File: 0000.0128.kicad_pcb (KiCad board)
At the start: 2 copper layers, 168 x 45.7 mm, 76 parts, among them J1 MicroMatch, J2 MicroMatch, J3 MicroMatch, J4 MicroMatch, J5 MicroMatch, J6 MicroMatch, J7 MicroMatch, J8 MicroMatch, U1 TL072, U2 TL072, U3 TL072, U4 TL072, U5 TL072, U6 TL072

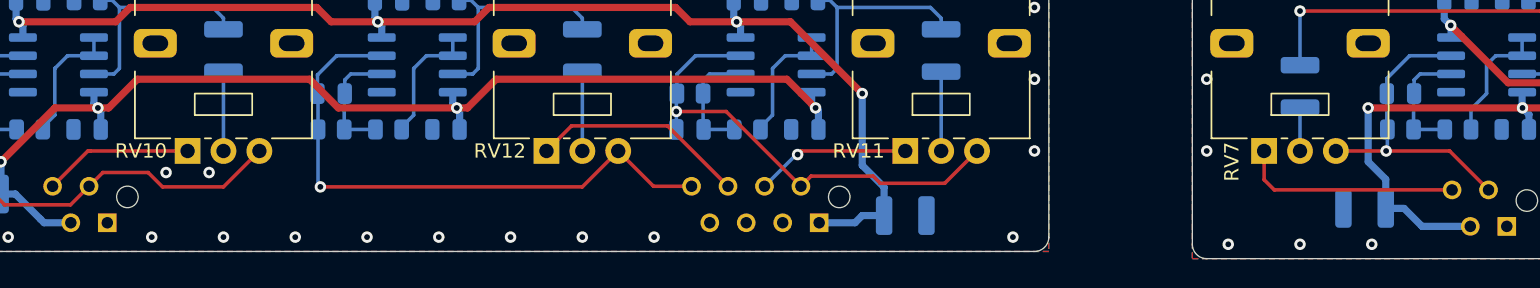
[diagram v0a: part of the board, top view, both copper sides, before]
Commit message: Oops, all of the single gang pots were backwards - fixed.
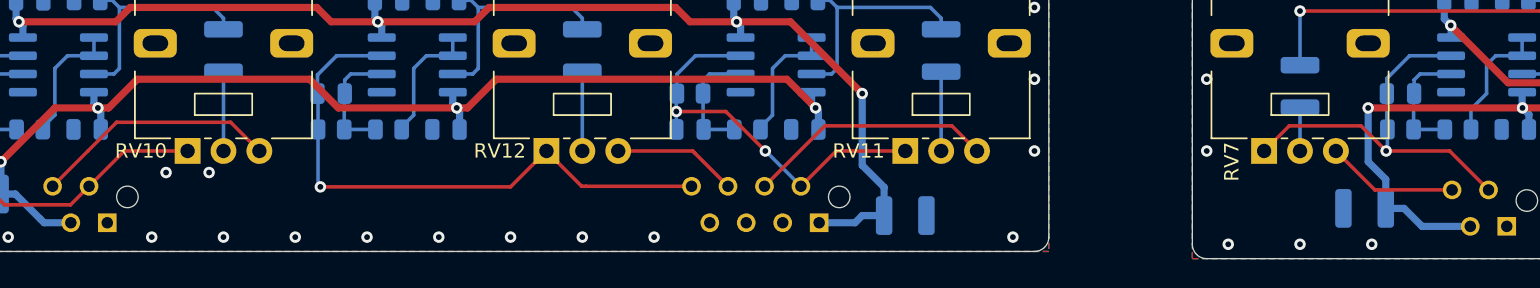
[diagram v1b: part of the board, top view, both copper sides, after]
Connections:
- RV10 pad 1: /Variant 4/SUB_IN -> /Variant 4/SUB_OUT
- RV10 pad 3: /Variant 4/SUB_OUT -> /Variant 4/SUB_IN
- RV11 pad 1: /Variant 4/CH1_IN -> /Variant 4/CH1_OUT
- RV11 pad 3: /Variant 4/CH1_OUT -> /Variant 4/CH1_IN
- RV12 pad 1: /Variant 4/CH2_IN -> /Variant 4/CH2_OUT
- RV12 pad 3: /Variant 4/CH2_OUT -> /Variant 4/CH2_IN
- RV7 pad 1: /Variant 3/SUB_IN -> /Variant 3/SUB_OUT
- RV7 pad 3: /Variant 3/SUB_OUT -> /Variant 3/SUB_IN
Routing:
- net /Variant 4/SUB_IN: track 10.4 -> 17.1 mm
- net /Variant 4/CH2_IN: track 15.1 -> 8.67 mm
- net /Variant 4/CH1_IN: track 10.8 -> 17.3 mm, vias 1 -> 0
- net /Variant 3/SUB_OUT: track 22.0 -> 28.4 mm
- net /Variant 3/SUB_IN: track 15.4 -> 9.22 mm
- net /Variant 4/SUB_OUT: track 35.5 -> 29.7 mm
- net /Variant 4/CH1_OUT: track 33.4 -> 28.0 mm, vias 1 -> 2
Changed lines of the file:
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@@
 			)
 			(remove_unused_layers no)
-			(net 76 "/Variant 4/SUB_IN")
+			(net 62 "/Variant 4/SUB_OUT")
 			(pinfunction "1")
 			(pintype "passive")
@@
 			)
 			(remove_unused_layers no)
-			(net 62 "/Variant 4/SUB_OUT")
+			(net 76 "/Variant 4/SUB_IN")
 			(pinfunction "3")
 			(pintype "passive")
@@
 			)
 			(remove_unused_layers no)
-			(net 32 "/Variant 3/SUB_IN")
+			(net 11 "/Variant 3/SUB_OUT")
 			(pinfunction "1")
 			(pintype "passive")
@@
 			)
 			(remove_unused_layers no)
-			(net 11 "/Variant 3/SUB_OUT")
+			(net 32 "/Variant 3/SUB_IN")
 			(pinfunction "3")
 			(pintype "passive")
@@
 			)
 			(remove_unused_layers no)
-			(net 74 "/Variant 4/CH2_IN")
+			(net 70 "/Variant 4/CH2_OUT")
 			(pinfunction "1")
 			(pintype "passive")
@@
 			)
 			(remove_unused_layers no)
-			(net 70 "/Variant 4/CH2_OUT")
+			(net 74 "/Variant 4/CH2_IN")
 			(pinfunction "3")
 			(pintype "passive")
@@
 			)
 			(remove_unused_layers no)
-			(net 75 "/Variant 4/CH1_IN")
+			(net 68 "/Variant 4/CH1_OUT")
 			(pinfunction "1")
 			(pintype "passive")
@@
 			)
 			(remove_unused_layers no)
-			(net 68 "/Variant 4/CH1_OUT")
+			(net 75 "/Variant 4/CH1_IN")
 			(pinfunction "3")
 			(pintype "passive")
@@
 		(tags "resistor")
 		(property "Reference" "R19"
-			(at 0 -1.75 0)
+			(at 0.5 -1.75 0)
 			(layer "B.SilkS")
 			(effects
@@
 	)
 	(segment
+		(start 152.5 110)
+		(end 154.25 108.25)
+		(width 0.25)
+		(layer "F.Cu")
+		(net 11)
+	)
+	(segment
 		(start 161 110)
 		(end 165.4225 110)
@@
 	)
 	(segment
-		(start 157.5 110)
+		(start 159.25 108.25)
 		(end 161 110)
 		(width 0.25)
@@
 		(net 11)
 	)
+	(segment
+		(start 154.25 108.25)
+		(end 159.25 108.25)
+		(width 0.25)
+		(layer "F.Cu")
+		(net 11)
+	)
 	(via
 		(at 161 110)
@@
 	)
 	(segment
-		(start 152.5 112)
-		(end 152.5 110)
-		(width 0.25)
-		(layer "F.Cu")
-		(net 32)
-	)
-	(segment
-		(start 165.595 112.7125)
-		(end 153.2125 112.7125)
+		(start 157.5 110)
+		(end 160.2125 112.7125)
 		(width 0.25)
 		(layer "F.Cu")
@@
 	)
 	(segment
-		(start 153.2125 112.7125)
-		(end 152.5 112)
+		(start 160.2125 112.7125)
+		(end 165.595 112.7125)
 		(width 0.25)
 		(layer "F.Cu")
@@
 	)
 	(segment
-		(start 71.595 111.5)
-		(end 74.75 111.5)
-		(width 0.25)
-		(layer "F.Cu")
-		(net 62)
-	)
-	(segment
-		(start 74.75 111.5)
-		(end 75.75 112.5)
-		(width 0.25)
-		(layer "F.Cu")
-		(net 62)
-	)
-	(segment
 		(start 70.635 112.46)
 		(end 69.345 113.75)
@@
 	)
 	(segment
-		(start 64.75 113.75)
-		(end 61.75 110.75)
-		(width 0.25)
-		(layer "F.Cu")
-		(net 62)
-	)
-	(segment
-		(start 75.75 112.5)
-		(end 80 112.5)
+		(start 77.5 110)
+		(end 73.095 110)
 		(width 0.25)
 		(layer "F.Cu")
@@
 	)
 	(segment
-		(start 80 112.5)
-		(end 82.5 110)
+		(start 64.75 113.75)
+		(end 61.75 110.75)
 		(width 0.25)
 		(layer "F.Cu")
@@
 	)
 	(segment
-		(start 70.635 112.46)
-		(end 71.595 111.5)
+		(start 73.095 110)
+		(end 70.635 112.46)
 		(width 0.25)
 		(layer "F.Cu")
@@
 	)
 	(segment
-		(start 120.94 111.75)
-		(end 125.25 111.75)
-		(width 0.25)
-		(layer "F.Cu")
-		(net 68)
-	)
-	(segment
-		(start 130.25 112.25)
-		(end 132.5 110)
+		(start 115 107.25)
+		(end 111.55 107.25)
 		(width 0.25)
 		(layer "F.Cu")
@@
 	)
 	(segment
-		(start 120.23 112.46)
-		(end 115.02 107.25)
+		(start 117.75 110)
+		(end 115 107.25)
 		(width 0.25)
 		(layer "F.Cu")
@@
 	)
 	(segment
-		(start 115.02 107.25)
-		(end 111.55 107.25)
+		(start 127.5 110)
+		(end 122.69 110)
 		(width 0.25)
 		(layer "F.Cu")
@@
 	)
 	(segment
-		(start 125.75 112.25)
-		(end 130.25 112.25)
+		(start 122.69 110)
+		(end 120.23 112.46)
 		(width 0.25)
 		(layer "F.Cu")
@@
 	)
 	(segment
-		(start 125.25 111.75)
-		(end 125.75 112.25)
+		(start 117.77 110)
+		(end 117.75 110)
 		(width 0.25)
 		(layer "F.Cu")
 		(net 68)
 	)
-	(segment
-		(start 120.23 112.46)
-		(end 120.94 111.75)
-		(width 0.25)
-		(layer "F.Cu")
+	(via
+		(at 111.55 107.25)
+		(size 0.8)
+		(drill 0.4)
+		(layers "F.Cu" "B.Cu")
 		(net 68)
 	)
 	(via
-		(at 111.55 107.25)
+		(at 117.75 110)
 		(size 0.8)
 		(drill 0.4)
@@
 	)
 	(segment
+		(start 117.77 110)
+		(end 120.23 112.46)
+		(width 0.25)
+		(layer "B.Cu")
+		(net 68)
+	)
+	(segment
 		(start 112.885 103.365)
 		(end 116.025 103.365)
@@
 	)
 	(segment
+		(start 117.75 110)
+		(end 117.77 110)
+		(width 0.25)
+		(layer "B.Cu")
+		(net 68)
+	)
+	(segment
 		(start 113.45 108.5)
 		(end 115.5875 108.5)
@@
 	)
 	(segment
-		(start 86.75 112.5)
-		(end 105 112.5)
+		(start 105.25 112.46)
+		(end 112.61 112.46)
 		(width 0.25)
 		(layer "F.Cu")
@@
 	)
 	(segment
-		(start 109.96 112.46)
-		(end 112.61 112.46)
+		(start 104.96 112.46)
+		(end 105.25 112.46)
 		(width 0.25)
 		(layer "F.Cu")
@@
 	)
 	(segment
-		(start 105 112.5)
-		(end 107.5 110)
+		(start 102.5 110)
+		(end 100 112.5)
 		(width 0.25)
 		(layer "F.Cu")
@@
 	)
 	(segment
-		(start 107.5 110)
-		(end 109.96 112.46)
+		(start 86.75 112.5)
+		(end 100 112.5)
+		(width 0.25)
+		(layer "F.Cu")
+		(net 70)
+	)
+	(segment
+		(start 102.5 110)
+		(end 104.96 112.46)
 		(width 0.25)
 		(layer "F.Cu")
@@
 	)
 	(segment
-		(start 104.25 108.25)
-		(end 102.5 110)
+		(start 107.5 110)
+		(end 112.69 110)
 		(width 0.25)
 		(layer "F.Cu")
@@
 	)
 	(segment
-		(start 110.94 108.25)
-		(end 104.25 108.25)
+		(start 115.15 112.46)
+		(end 112.845 110.155)
 		(width 0.25)
 		(layer "F.Cu")
@@
 	)
 	(segment
-		(start 115.15 112.46)
-		(end 110.94 108.25)
+		(start 112.69 110)
+		(end 112.845 110.155)
 		(width 0.25)
 		(layer "F.Cu")
@@
 	)
 	(segment
-		(start 120 110.25)
-		(end 120.25 110)
+		(start 130.75 108.25)
+		(end 132.5 110)
 		(width 0.25)
 		(layer "F.Cu")
@@
 	)
 	(segment
-		(start 120.25 110)
-		(end 127.5 110)
+		(start 121.9 108.25)
+		(end 130.75 108.25)
 		(width 0.25)
 		(layer "F.Cu")
 		(net 75)
 	)
-	(via
-		(at 120 110.25)
-		(size 0.8)
-		(drill 0.4)
-		(layers "F.Cu" "B.Cu")
-		(net 75)
-	)
 	(segment
-		(start 119.9 110.25)
-		(end 120 110.25)
+		(start 117.69 112.46)
+		(end 121.9 108.25)
 		(width 0.25)
-		(layer "B.Cu")
+		(layer "F.Cu")
 		(net 75)
 	)
 	(segment
-		(start 117.69 112.46)
-		(end 119.9 110.25)
+		(start 82.5 110)
+		(end 80.5 108)
 		(width 0.25)
-		(layer "B.Cu")
-		(net 75)
+		(layer "F.Cu")
+		(net 76)
 	)
 	(segment
-		(start 70.555 110)
-		(end 70.75 110)
+		(start 72.555 108)
+		(end 70.555 110)
 		(width 0.25)
 		(layer "F.Cu")
@@
 	)
 	(segment
-		(start 77.5 110)
-		(end 70.75 110)
+		(start 80.5 108)
+		(end 72.555 108)
 		(width 0.25)
 		(layer "F.Cu")

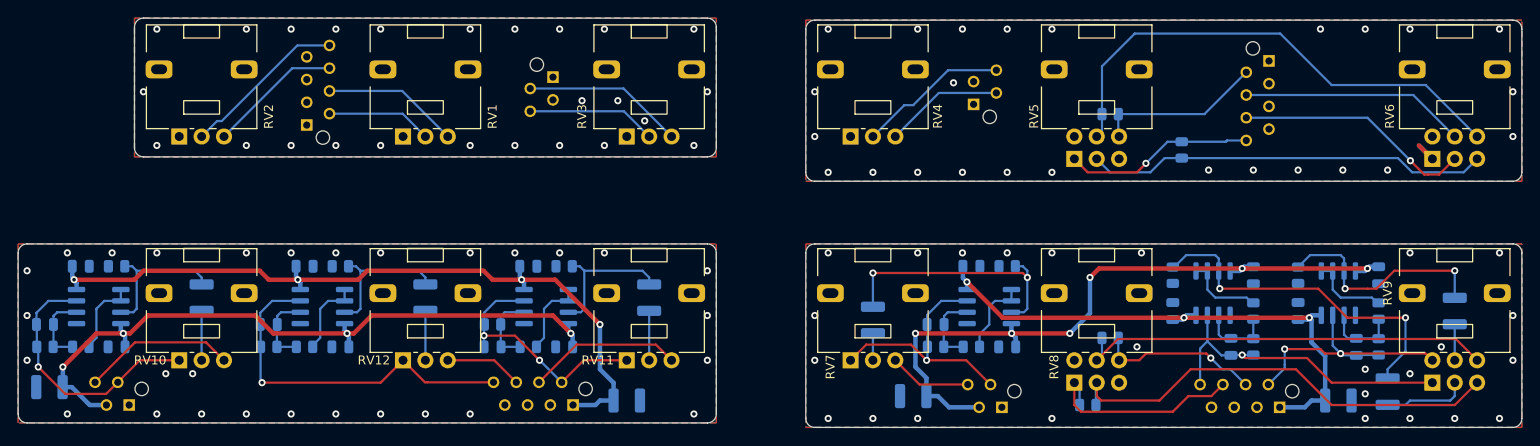
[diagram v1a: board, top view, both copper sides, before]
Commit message: Active control topology changed to a single op-amp version.
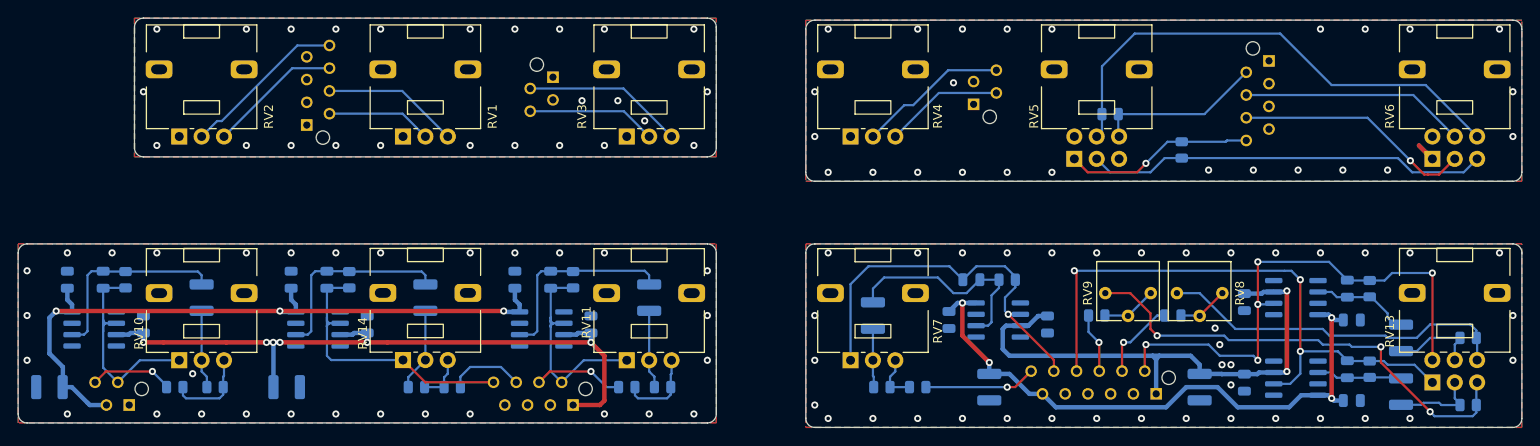
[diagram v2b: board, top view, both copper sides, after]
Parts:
- removed C27, C28: 151, Capacitor_SMD:C_0805_2012Metric
- removed J5: MicroMatch, Connector_TE-Connectivity:TE_Micro-MaTch_215079-8_2x04_P1.27mm_Vertical
- removed J6: MicroMatch, Connector_TE-Connectivity:TE_Micro-MaTch_215079-4_2x02_P1.27mm_Vertical
- removed R20: 3K, Resistor_SMD:R_0805_2012Metric
- removed R21, R22: 15K, Resistor_SMD:R_0805_2012Metric
- removed RV12: 10K, Potentiometer_THT:Potentiometer_Alps_RK09L_Single_Vertical
- removed U4, U5, U6: TL072, Package_SO:SOIC-8_3.9x4.9mm_P1.27mm
- added C29: 106, Capacitor_SMD:C_1210_3225Metric, B.Cu at (105.0, 103.0)
- added C30: 151, Capacitor_SMD:C_0805_2012Metric, B.Cu at (94.0, 101.0)
- added J9: MicroMatch, Connector_TE-Connectivity:TE_Micro-MaTch_1-215079-2_2x06_P1.27mm_Vertical, B.Cu at (186.6, 113.8)
- added R23: 100K, Resistor_SMD:R_0805_2012Metric, B.Cu at (96.5, 101.0)
- added RV13: 10K, Potentiometer_THT:Potentiometer_Alps_RK09L_Double_Vertical, F.Cu at (217.5, 112.5)
- added RV14: 10K LIN, Potentiometer_THT:Potentiometer_Alps_RK09L_Single_Vertical, F.Cu at (102.5, 110.0)
- added U7: TL071, Package_SO:SOIC-8_3.9x4.9mm_P1.27mm, B.Cu at (93.0, 106.5)
- added U8: TL071, Package_SO:SOIC-8_3.9x4.9mm_P1.27mm, B.Cu at (68.0, 106.5)
- added U9: TL071, Package_SO:SOIC-8_3.9x4.9mm_P1.27mm, B.Cu at (118.0, 106.5)
- C1, C11, C12, C15, C25: value 105 -> 106
- C26: value 105 -> 151; footprint Capacitor_SMD:C_1210_3225Metric -> Capacitor_SMD:C_0805_2012Metric
- R10, R11, R19: value 3K -> 100K
- R12: value 15K -> 3K
- R13, R5: value 15K -> 22K
- R14, R17: value 100K -> 3K
- R15: value 3K -> 22K
- R16: value 15K -> 100K
- R18, R8, R9: value 100K -> 22K
- R6, R7: value R -> 3K
- RV10, RV11, RV7: value 10K -> 10K LIN
- RV8, RV9: value 10K -> 1K; footprint Potentiometer_THT:Potentiometer_Alps_RK09L_Double_Vertical -> HR_parts:Potentiometer_Bourns_3362P_Vertical
- U1, U2, U3: value TL072 -> TL071
- moved R12 103.6 mm to (108.0, 113.0), turned to 180 degrees
- moved R13 93.6 mm to (104.0, 113.0), turned to 180 degrees
- moved R18 38.4 mm to (131.5, 113.0), turned to 180 degrees
- moved C23 38.0 mm to (89.5, 113.0)
- moved R9 36.0 mm to (221.5, 115.0), turned to 180 degrees
- moved RV9 35.4 mm to (183.5, 102.5), turned to -90 degrees
- moved R8 20.2 mm to (221.5, 107.5), turned to 180 degrees
- moved C4 17.8 mm to (208.5, 114.5), turned to 180 degrees
- moved RV8 17.2 mm to (191.5, 102.5), turned to -90 degrees
- moved R15 15.7 mm to (81.5, 113.0)
- moved C9 15.6 mm to (191.5, 113.0), turned to -90 degrees
- moved R17 15.2 mm to (127.5, 113.0)
- moved R14 15.0 mm to (77.0, 113.0)
- moved R11 14.5 mm to (210.5, 111.0)
- moved C26 14.1 mm to (119.0, 101.0), turned to -90 degrees
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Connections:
- C1 pad 2: Net-(U1A-+) -> Net-(U1--)
- C11 pad 2: Net-(U2A-+) -> Net-(U2--)
- C12 pad 2: Net-(U3A-+) -> Net-(U3--)
- C13 pad 1: Net-(U2B--) -> Net-(U2--)
- C14 pad 1: Net-(U3B--) -> Net-(U3--)
- C15 pad 2: Net-(U4A-+) -> Net-(U8--)
- C16 pad 1: Net-(U4B--) -> Net-(U8--)
- C2 pad 1: Net-(U1B--) -> Net-(U1--)
- C25 pad 2: Net-(U5A-+) -> Net-(U9--)
- C26 pad 1: Net-(C26-Pad1) -> Net-(U9--)
- C26 pad 2: Net-(U6A-+) -> /Variant 4/CH1_OUT
- R10 pad 1: Net-(U2A--) -> /Variant 3/CH1_OUT
- R10 pad 2: Net-(U2B--) -> Net-(U2--)
- R11 pad 1: Net-(U3A--) -> /Variant 3/CH2_OUT
- R11 pad 2: Net-(U3B--) -> Net-(U3--)
- R12 pad 1: Net-(U2B--) -> /Variant 4/CH2_IN
- R12 pad 2: /Variant 3/CH1_OUT -> Net-(R12-Pad2)
- R13 pad 1: Net-(U3B--) -> Net-(R12-Pad2)
- R13 pad 2: /Variant 3/CH2_OUT -> Net-(C29-Pad1)
- R14 pad 1: GND3 -> /Variant 4/SUB_IN
- R14 pad 2: Net-(U4A-+) -> Net-(R14-Pad2)
- R15 pad 1: Net-(U4A--) -> Net-(R14-Pad2)
- R15 pad 2: Net-(U4B--) -> Net-(C15-Pad1)
- R16 pad 1: Net-(U4B--) -> /Variant 4/SUB_OUT
- R16 pad 2: /Variant 4/SUB_OUT -> Net-(U8--)
- R17 pad 1: GND3 -> /Variant 4/CH1_IN
- R17 pad 2: Net-(U5A-+) -> Net-(R17-Pad2)
- R18 pad 1: GND3 -> Net-(R17-Pad2)
- R18 pad 2: Net-(U6A-+) -> Net-(C25-Pad1)
- R19 pad 1: Net-(U5A--) -> /Variant 4/CH1_OUT
- R19 pad 2: Net-(U5B--) -> Net-(U9--)
- R3 pad 1: GND1 -> /Variant 3/SUB_OUT
- R3 pad 2: Net-(U1A-+) -> Net-(U1--)
- R4 pad 1: Net-(U1A--) -> /Variant 3/SUB_IN
- R4 pad 2: Net-(U1B--) -> Net-(R4-Pad2)
- R5 pad 1: Net-(U1B--) -> Net-(R4-Pad2)
- R5 pad 2: /Variant 3/SUB_OUT -> Net-(C1-Pad1)
- R8 pad 1: GND1 -> Net-(R8-Pad1)
- R8 pad 2: Net-(U2A-+) -> Net-(C11-Pad1)
- R9 pad 1: GND1 -> Net-(R9-Pad1)
- R9 pad 2: Net-(U3A-+) -> Net-(C12-Pad1)
- RV10 pad 3: /Variant 4/SUB_IN -> Net-(R14-Pad2)
- RV11 pad 3: /Variant 4/CH1_IN -> Net-(R17-Pad2)
- RV7 pad 3: /Variant 3/SUB_IN -> Net-(R4-Pad2)
- RV8 pad 1: /Variant 3/CH2_IN -> Net-(R8-Pad1)
- RV8 pad 2: Net-(R7-Pad2) -> Net-(R6-Pad2)
- RV8 pad 3: GND1 -> Net-(R6-Pad2)
- RV9 pad 1: /Variant 3/CH2_OUT -> Net-(R9-Pad1)
- RV9 pad 2: Net-(C12-Pad1) -> Net-(R7-Pad2)
- U1 pad 1: Net-(U1A--) -> unconnected-(U1-NULL-Pad1)
- U1 pad 2: Net-(U1A--) -> Net-(U1--)
- U1 pad 3: Net-(U1A-+) -> GND1
- U1 pad 5: GND1 -> unconnected-(U1-NULL-Pad5)
- U1 pad 6: Net-(U1B--) -> /Variant 3/SUB_OUT
- U1 pad 7: /Variant 3/SUB_OUT -> +15V
- U1 pad 8: +15V -> unconnected-(U1-NC-Pad8)
- U2 pad 1: Net-(U2A--) -> unconnected-(U2-NULL-Pad1)
- U2 pad 2: Net-(U2A--) -> Net-(U2--)
- U2 pad 3: Net-(U2A-+) -> GND1
- U2 pad 5: GND1 -> unconnected-(U2-NULL-Pad5)
- U2 pad 6: Net-(U2B--) -> /Variant 3/CH1_OUT
- U2 pad 7: /Variant 3/CH1_OUT -> +15V
- U2 pad 8: +15V -> unconnected-(U2-NC-Pad8)
- U3 pad 1: Net-(U3A--) -> unconnected-(U3-NULL-Pad1)
- U3 pad 2: Net-(U3A--) -> Net-(U3--)
- U3 pad 3: Net-(U3A-+) -> GND1
- U3 pad 5: GND1 -> unconnected-(U3-NULL-Pad5)
- U3 pad 6: Net-(U3B--) -> /Variant 3/CH2_OUT
- U3 pad 7: /Variant 3/CH2_OUT -> +15V
- U3 pad 8: +15V -> unconnected-(U3-NC-Pad8)
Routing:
- net Net-(R9-Pad1): track 0.00 -> 52.8 mm, vias 0 -> 3
- net Net-(R7-Pad2): track 50.9 -> 6.20 mm
- net Net-(R6-Pad2): track 47.2 -> 5.70 mm
- net Net-(R8-Pad1): track 0.00 -> 39.8 mm
- net Net-(U3A-+): track 39.0 -> 0.00 mm, vias 2 -> 0
- net /Variant 3/CH2_OUT: track 36.4 -> 67.3 mm, vias 1 -> 3
- net Net-(U1A-+): track 29.0 -> 0.00 mm, vias 2 -> 0
- net /Variant 3/CH1_OUT: track 30.7 -> 59.5 mm, vias 2 -> 5
- net Net-(U2A-+): track 25.4 -> 0.00 mm, vias 2 -> 0
- net Net-(U1--): track 0.00 -> 24.5 mm
- net Net-(U9--): track 0.00 -> 22.4 mm
- net Net-(U8--): track 0.00 -> 22.3 mm
- net Net-(U7--): track 0.00 -> 22.3 mm
- net /Variant 3/CH2_IN: track 23.4 -> 6.71 mm, vias 0 -> 1
- net Net-(U5A-+): track 16.1 -> 0.00 mm
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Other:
- board text added: "Variant 3: Active volume/trim"
- board text removed: "Variant 3: Active volume/balance"
